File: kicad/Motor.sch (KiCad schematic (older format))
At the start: 8 parts, among them J1 Motor_L, J2 Motor_R, U2 DRV8835

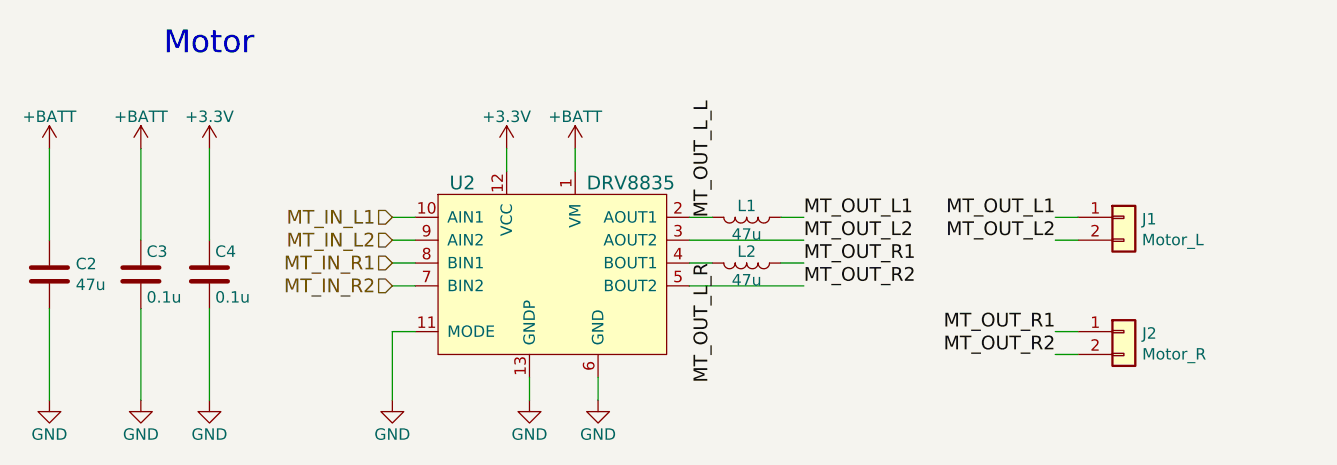
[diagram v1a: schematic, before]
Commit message: エンコーダー基板の位置を調整
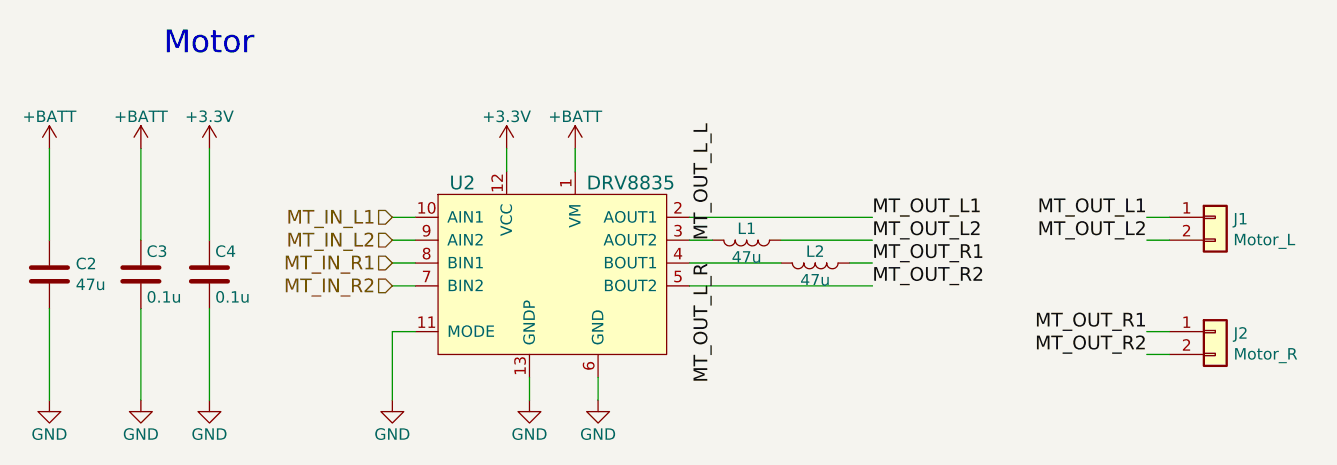
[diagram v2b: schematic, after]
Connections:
- net MT_OUT_L1: now also U2.2 (AOUT1); no longer L1.1
- net MT_OUT_L2: now also L1.1; no longer U2.3 (AOUT2)
- net MT_OUT_L_L: now also U2.3 (AOUT2); no longer U2.2 (AOUT1)
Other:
- moved on the sheet: J1, J2, L1, L2
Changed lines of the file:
@@
 	1    0    0    -1
 $EndComp
-Text Label 6600 3400 0    60   ~ 0
+Text Label 6900 3400 0    60   ~ 0
 MT_OUT_L1
-Text Label 6600 3500 0    60   ~ 0
+Text Label 6900 3500 0    60   ~ 0
 MT_OUT_L2
 Text HLabel 4800 3400 0    60   Input ~ 0
@@
 	1    0    0    -1
 $EndComp
-Text Label 6600 3600 0    60   ~ 0
+Text Label 6900 3600 0    60   ~ 0
 MT_OUT_R1
-Text Label 6600 3700 0    60   ~ 0
+Text Label 6900 3700 0    60   ~ 0
 MT_OUT_R2
 Text HLabel 4800 3600 0    60   Input ~ 0
@@
 Text HLabel 4800 3700 0    60   Input ~ 0
 MT_IN_R2
-Text Label 7700 3400 2    60   ~ 0
+Text Label 8100 3400 2    60   ~ 0
 MT_OUT_L1
-Text Label 7700 3500 2    60   ~ 0
+Text Label 8100 3500 2    60   ~ 0
 MT_OUT_L2
-Text Label 7700 3900 2    60   ~ 0
+Text Label 8100 3900 2    60   ~ 0
 MT_OUT_R1
-Text Label 7700 4000 2    60   ~ 0
+Text Label 8100 4000 2    60   ~ 0
 MT_OUT_R2
 $Comp
@@
 L Device:L L1
 U 1 1 5B66FC72
-P 6350 3400
-F 0 "L1" V 6300 3400 50  0000 C CNN
-F 1 "47u" V 6425 3400 50  0000 C CNN
-F 2 "mouse:L_4018" H 6350 3400 50  0001 C CNN
-F 3 "" H 6350 3400 50  0001 C CNN
-	1    6350 3400
+P 6350 3500
+F 0 "L1" V 6300 3500 50  0000 C CNN
+F 1 "47u" V 6425 3500 50  0000 C CNN
+F 2 "mouse:L_4018" H 6350 3500 50  0001 C CNN
+F 3 "" H 6350 3500 50  0001 C CNN
+	1    6350 3500
 	0    1    1    0
 $EndComp
@@
 L Device:L L2
 U 1 1 5B66FD2C
-P 6350 3600
-F 0 "L2" V 6300 3600 50  0000 C CNN
-F 1 "47u" V 6425 3600 50  0000 C CNN
-F 2 "mouse:L_4018" H 6350 3600 50  0001 C CNN
-F 3 "" H 6350 3600 50  0001 C CNN
-	1    6350 3600
+P 6650 3600
+F 0 "L2" V 6600 3600 50  0000 C CNN
+F 1 "47u" V 6725 3600 50  0000 C CNN
+F 2 "mouse:L_4018" H 6650 3600 50  0001 C CNN
+F 3 "" H 6650 3600 50  0001 C CNN
+	1    6650 3600
 	0    1    1    0
 $EndComp
@@
 	4000 3800 4000 4200
 Wire Wire Line
-	6200 3400 6100 3400
-Wire Wire Line
-	6100 3500 6600 3500
-Wire Wire Line
 	4800 3400 4900 3400
 Wire Wire Line
@@
 	4900 3700 4800 3700
 Wire Wire Line
-	7700 4000 7800 4000
-Wire Wire Line
-	7800 3900 7700 3900
-Wire Wire Line
-	7700 3400 7800 3400
-Wire Wire Line
-	7800 3500 7700 3500
+	8100 4000 8200 4000
+Wire Wire Line
+	8200 3900 8100 3900
+Wire Wire Line
+	8100 3400 8200 3400
+Wire Wire Line
+	8200 3500 8100 3500
 Wire Wire Line
 	3700 4200 3700 3800
 Wire Wire Line
 	3700 3500 3700 3100
-Wire Wire Line
-	6600 3400 6500 3400
-Text Label 6200 3400 1    60   ~ 0
+Text Label 6200 3500 1    60   ~ 0
 MT_OUT_L_L
 Text Label 6200 3600 3    60   ~ 0
@@
 L Connector_Generic:Conn_01x02 J1
 U 1 1 5B6F504A
-P 8000 3400
-F 0 "J1" H 8079 3392 50  0000 L CNN
-F 1 "Motor_L" H 8079 3301 50  0000 L CNN
-F 2 "mouse:SMD_conn_2" H 8000 3400 50  0001 C CNN
-F 3 "~" H 8000 3400 50  0001 C CNN
-	1    8000 3400
+P 8400 3400
+F 0 "J1" H 8479 3392 50  0000 L CNN
+F 1 "Motor_L" H 8479 3301 50  0000 L CNN
+F 2 "mouse:SMD_conn_2" H 8400 3400 50  0001 C CNN
+F 3 "~" H 8400 3400 50  0001 C CNN
+	1    8400 3400
 	1    0    0    -1
 $EndComp
@@
 L Connector_Generic:Conn_01x02 J2
 U 1 1 5B6F50A6
-P 8000 3900
-F 0 "J2" H 8080 3892 50  0000 L CNN
-F 1 "Motor_R" H 8080 3801 50  0000 L CNN
-F 2 "mouse:SMD_conn_2" H 8000 3900 50  0001 C CNN
-F 3 "~" H 8000 3900 50  0001 C CNN
-	1    8000 3900
+P 8400 3900
+F 0 "J2" H 8480 3892 50  0000 L CNN
+F 1 "Motor_R" H 8480 3801 50  0000 L CNN
+F 2 "mouse:SMD_conn_2" H 8400 3900 50  0001 C CNN
+F 3 "~" H 8400 3900 50  0001 C CNN
+	1    8400 3900
 	1    0    0    -1
 $EndComp
@@
 	1    0    0    -1
 $EndComp
-Wire Wire Line
-	6200 3600 6100 3600
-Wire Wire Line
-	6100 3700 6600 3700
-Wire Wire Line
-	6500 3600 6600 3600
 $Comp
 L Device:C C2
@@
 Wire Wire Line
 	3300 3100 3300 3500
+Wire Wire Line
+	6200 3500 6100 3500
+Wire Wire Line
+	6800 3600 6900 3600
+Wire Wire Line
+	6500 3500 6900 3500
+Wire Wire Line
+	6100 3400 6900 3400
+Wire Wire Line
+	6100 3700 6900 3700
+Wire Wire Line
+	6100 3600 6500 3600
 $EndSCHEMATC
